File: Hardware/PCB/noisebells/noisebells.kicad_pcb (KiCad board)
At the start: 2 copper layers, 96 x 144 mm, 50 parts, among them J1 Synth_power_2x5, J2 Conn_01x05, Q1 2N3904, Q2 2N3904, SW1 SW_DPDT_x2, SW2 SW_DPDT_x2, U1 40106, U2 4070, U3 4066

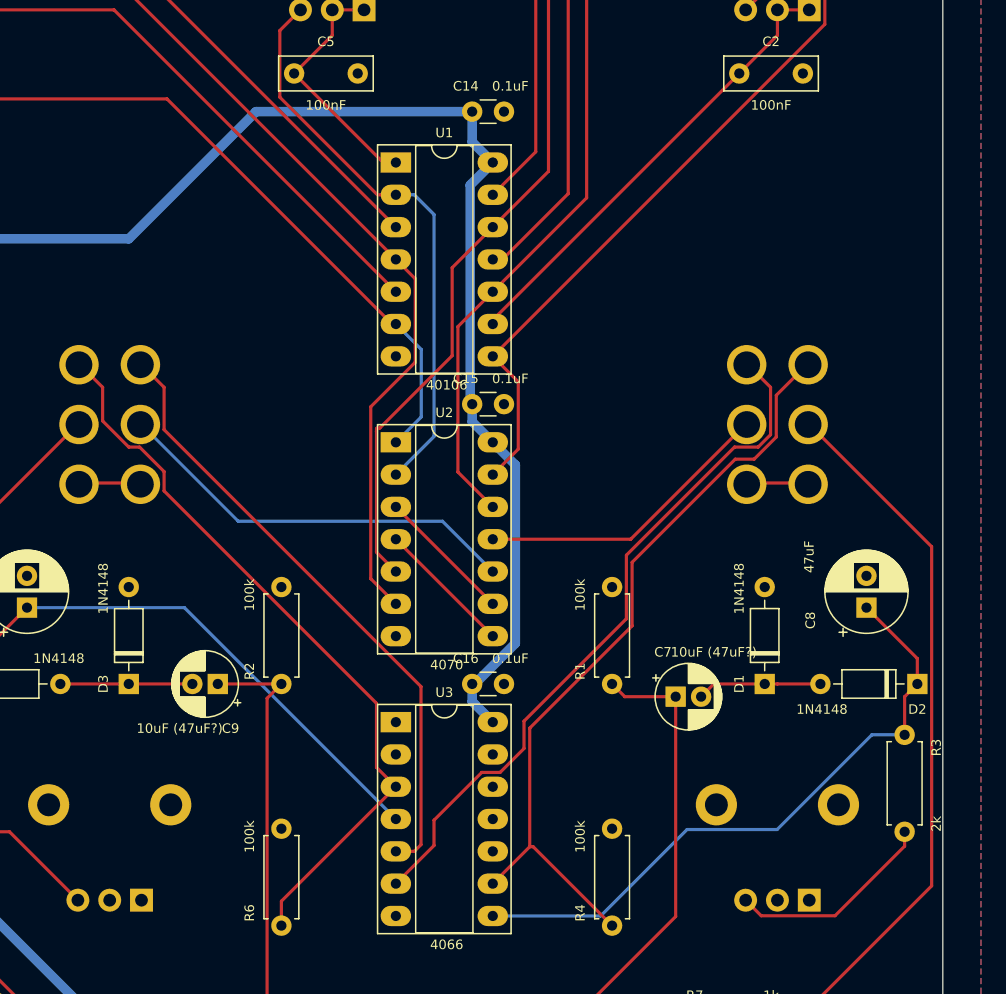
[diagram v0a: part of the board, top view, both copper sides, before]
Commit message: Correct caps value; fix wrong pot direction; move resistor label
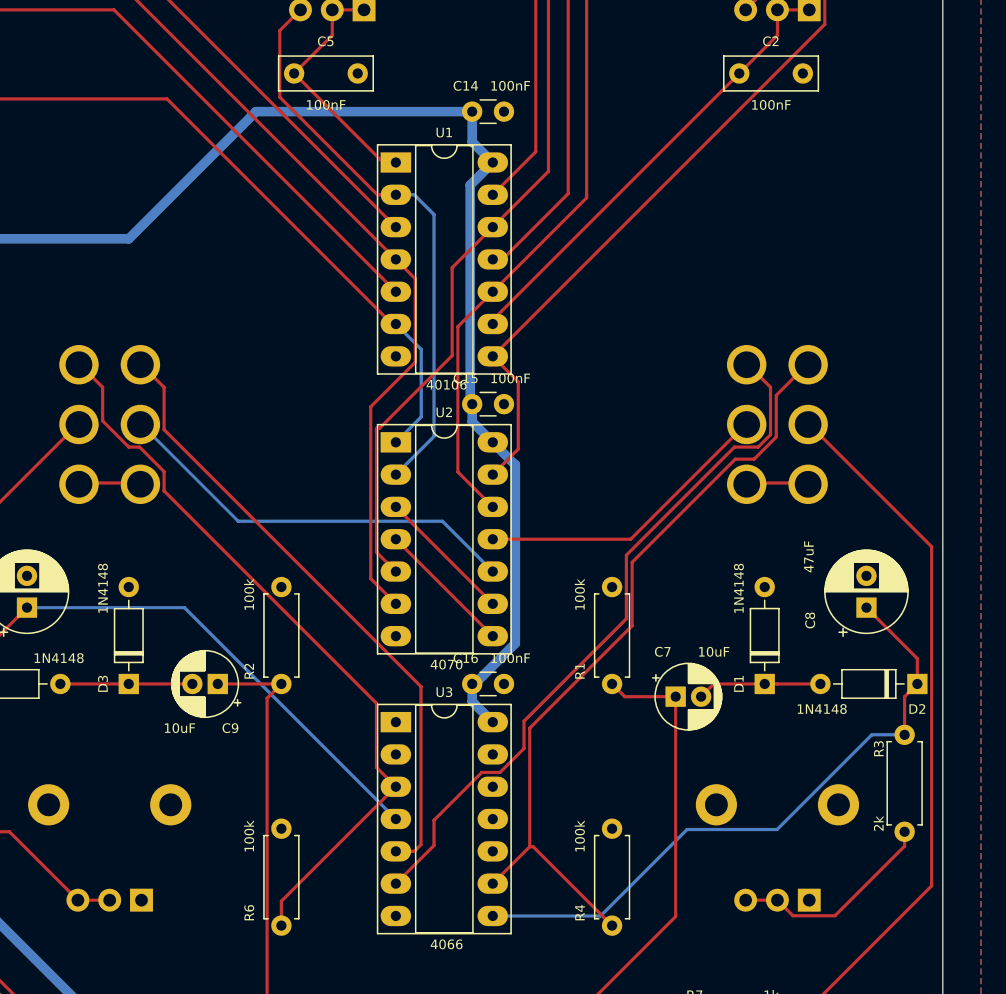
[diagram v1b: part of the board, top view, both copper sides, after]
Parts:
- C14, C15, C16: value 0.1uF -> 100nF
- C7, C9: value 10uF (47uF?) -> 10uF
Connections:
- RV7 pad 2: GND -> Net-(R3-Pad2)
- RV8 pad 2: GND -> Net-(R5-Pad2)
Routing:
- net Net-(R5-Pad2): track 11.2 -> 13.7 mm

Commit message: Add credit to Williams
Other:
- board text added: "Based on a design by Elliot Williams https://hackaday.com/2015/04/10/logic-noise-more-cmos-cowbell"
